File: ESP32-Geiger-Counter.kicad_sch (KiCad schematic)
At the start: 0 parts

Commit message: save
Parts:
- added J1: USB_C_Receptacle_PowerOnly_6P, symbol Connector:USB_C_Receptacle_PowerOnly_6P
- added U1: TP4056-42-ESOP8, Package_SO:SOIC-8-1EP_3.9x4.9mm_P1.27mm_EP2.41x3.3mm_ThermalVias, symbol Battery_Management:TP4056-42-ESOP8
- added U2: ESP32-WROOM-32, RF_Module:ESP32-WROOM-32, symbol RF_Module:ESP32-WROOM-32
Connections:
- new net: U2.1 (GND), U2.15 (GND), U2.38 (GND), U2.39 (GND)
- new net: J1.A12 (GND), J1.B12 (GND)
- new net: J1.A9 (VBUS), J1.B9 (VBUS)
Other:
- title: (none) -> ESP32-based Geiger Counter

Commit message: usb
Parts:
- removed J1: USB_C_Receptacle_PowerOnly_6P, symbol Connector:USB_C_Receptacle_PowerOnly_6P
- added BT1: Battery_Cell, Connector_JST:JST_PH_B2B-PH-K_1x02_P2.00mm_Vertical, symbol Device:Battery_Cell
- added J1: USB_C_Receptacle_USB2.0_16P, symbol Connector:USB_C_Receptacle_USB2.0_16P
- added R1, R2: 5.1K, symbol Device:R
- added U3: CP2102N-Axx-xQFN20, Package_DFN_QFN:SiliconLabs_QFN-20-1EP_3x3mm_P0.5mm, symbol Interface_USB:CP2102N-Axx-xQFN20
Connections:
- new net: J1.B5 (CC2), R2.1
- new net: J1.A5 (CC1), R1.1
- new net: U3.12 (GND), U3.21 (GND), U3.3 (GND)
- new net +3.3V: BT1.1 (+)
- new net +5V: J1.A4 (VBUS), J1.A9 (VBUS), J1.B4 (VBUS), J1.B9 (VBUS), U3.8 (VBUS)
- new net D+: J1.A6 (D+), J1.B6 (D+), U3.4 (D+)
- new net D-: J1.A7 (D-), J1.B7 (D-), U3.5 (D-)
- new net GND: BT1.2 (-), J1.A1 (GND), J1.A12 (GND), J1.B1 (GND), J1.B12 (GND), J1.SH (SHIELD), R1.2, R2.2
- no-connect marks 0 -> 2
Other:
- note added: "3.7V Lipo Cell"
- moved on the sheet: U1, U2

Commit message: saving
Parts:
- added C2: 10uF, symbol Device:C
- added C3: 100nF, symbol Device:C
- added F1: Polyfuse 500mA, Fuse:Fuse_1812_4532Metric, symbol Device:Polyfuse
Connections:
- net +5V: now also F1.1; no longer U3.8 (VBUS)
- net GND: now also U1.3 (GND), U1.9 (EPAD), C2.2, C3.2
- net VBUS_FUSED: now reaches U1.4 (V_{CC})
- net VBUS_FUSED: now also C2.1, C3.1, F1.2
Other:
- note added: "USB Input"
- moved on the sheet: BT1, U1, U2, U3

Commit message: working on TP4056
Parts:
- added D1: Red LED, symbol Device:LED
- added D2: Green LED, symbol Device:LED
- added R4: 2K, symbol Device:R
- added R5: 10K, symbol Device:R
- added R6, R7: 1K, symbol Device:R
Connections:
- net +3.3V is gone; now on net VBAT: BT1.1 (+)
- net VBUS_FUSED is gone; now on net +5V: C2.1, C3.1, F1.2, U1.4 (V_{CC})
- net +5V: now also U1.8 (CE), D1.2 (A), D2.2 (A), R5.2; no longer F1.1, J1.A4 (VBUS), J1.A9 (VBUS), J1.B4 (VBUS), J1.B9 (VBUS)
- net GND: now also R4.2
- net at U1.1 (TEMP): now also R5.1
- net at U1.2 (PROG): now also R4.1
- net VBAT: now reaches U1.5 (BAT)
- net at U1.6 (~{STDBY}): now also R7.2
- net at U1.7 (~{CHRG}): now also R6.2
- new net: D2.1 (K), R7.1
- new net: F1.1, J1.A4 (VBUS), J1.A9 (VBUS), J1.B4 (VBUS), J1.B9 (VBUS)
- new net: D1.1 (K), R6.1
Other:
- moved on the sheet: C2, C3, F1, U1, U2, U3

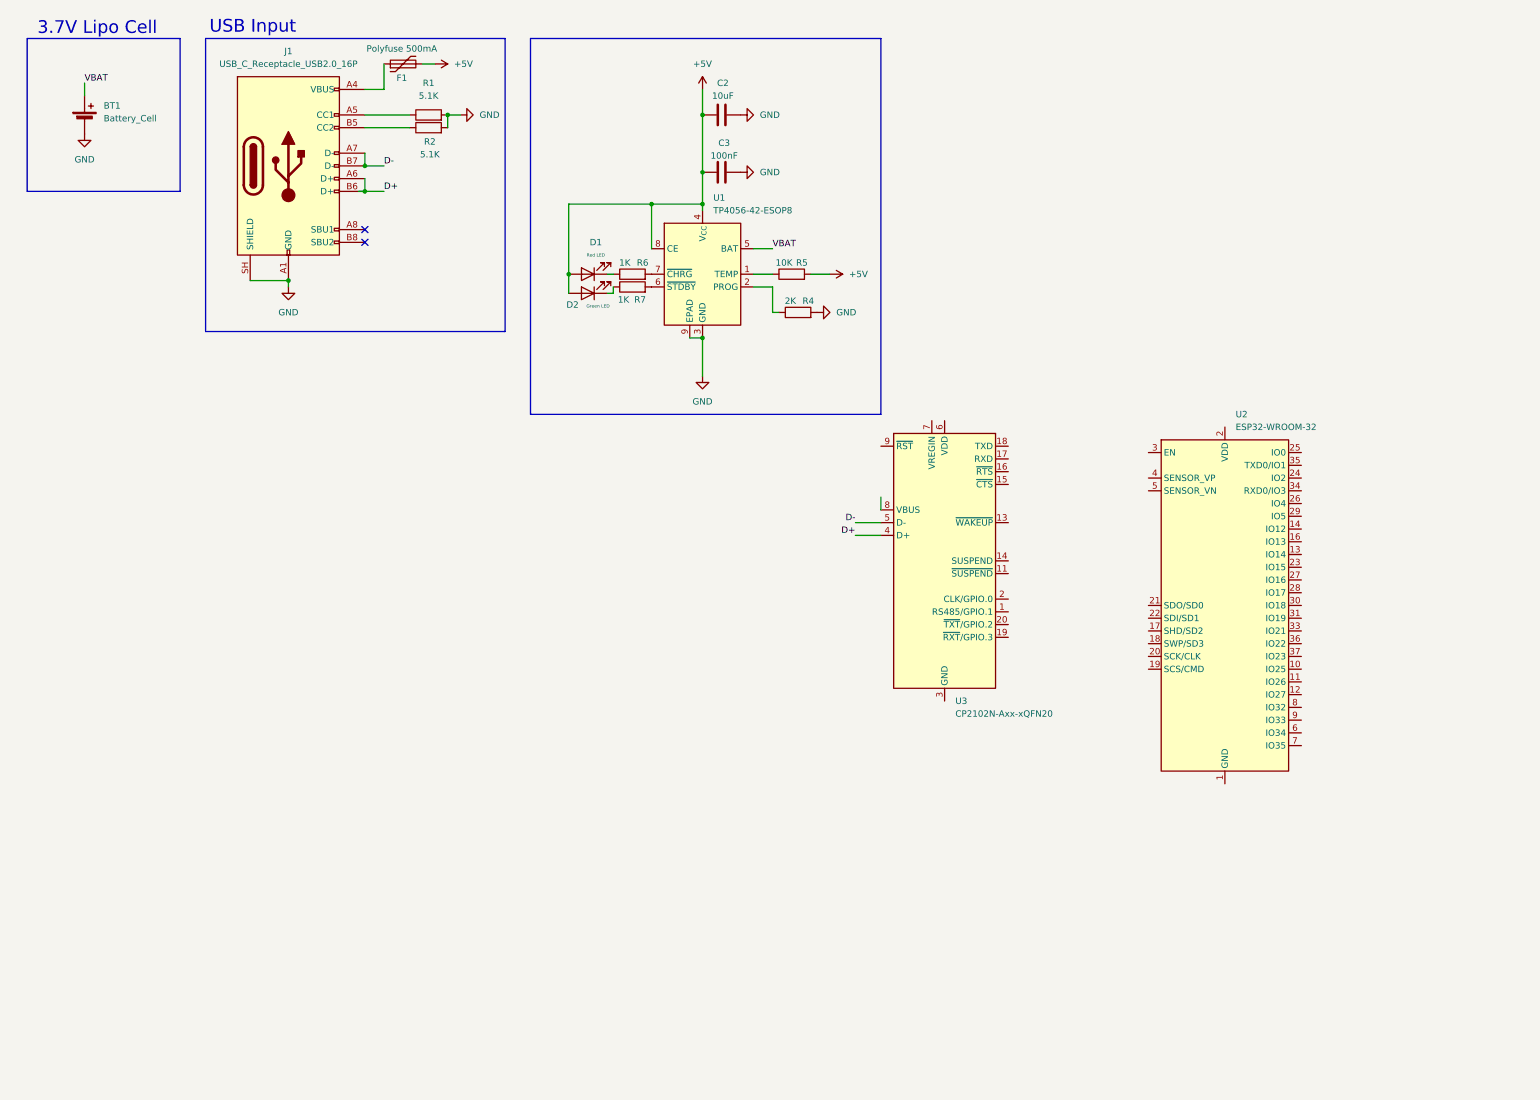
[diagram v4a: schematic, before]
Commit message: Lipo charging + usb input + lipo cell
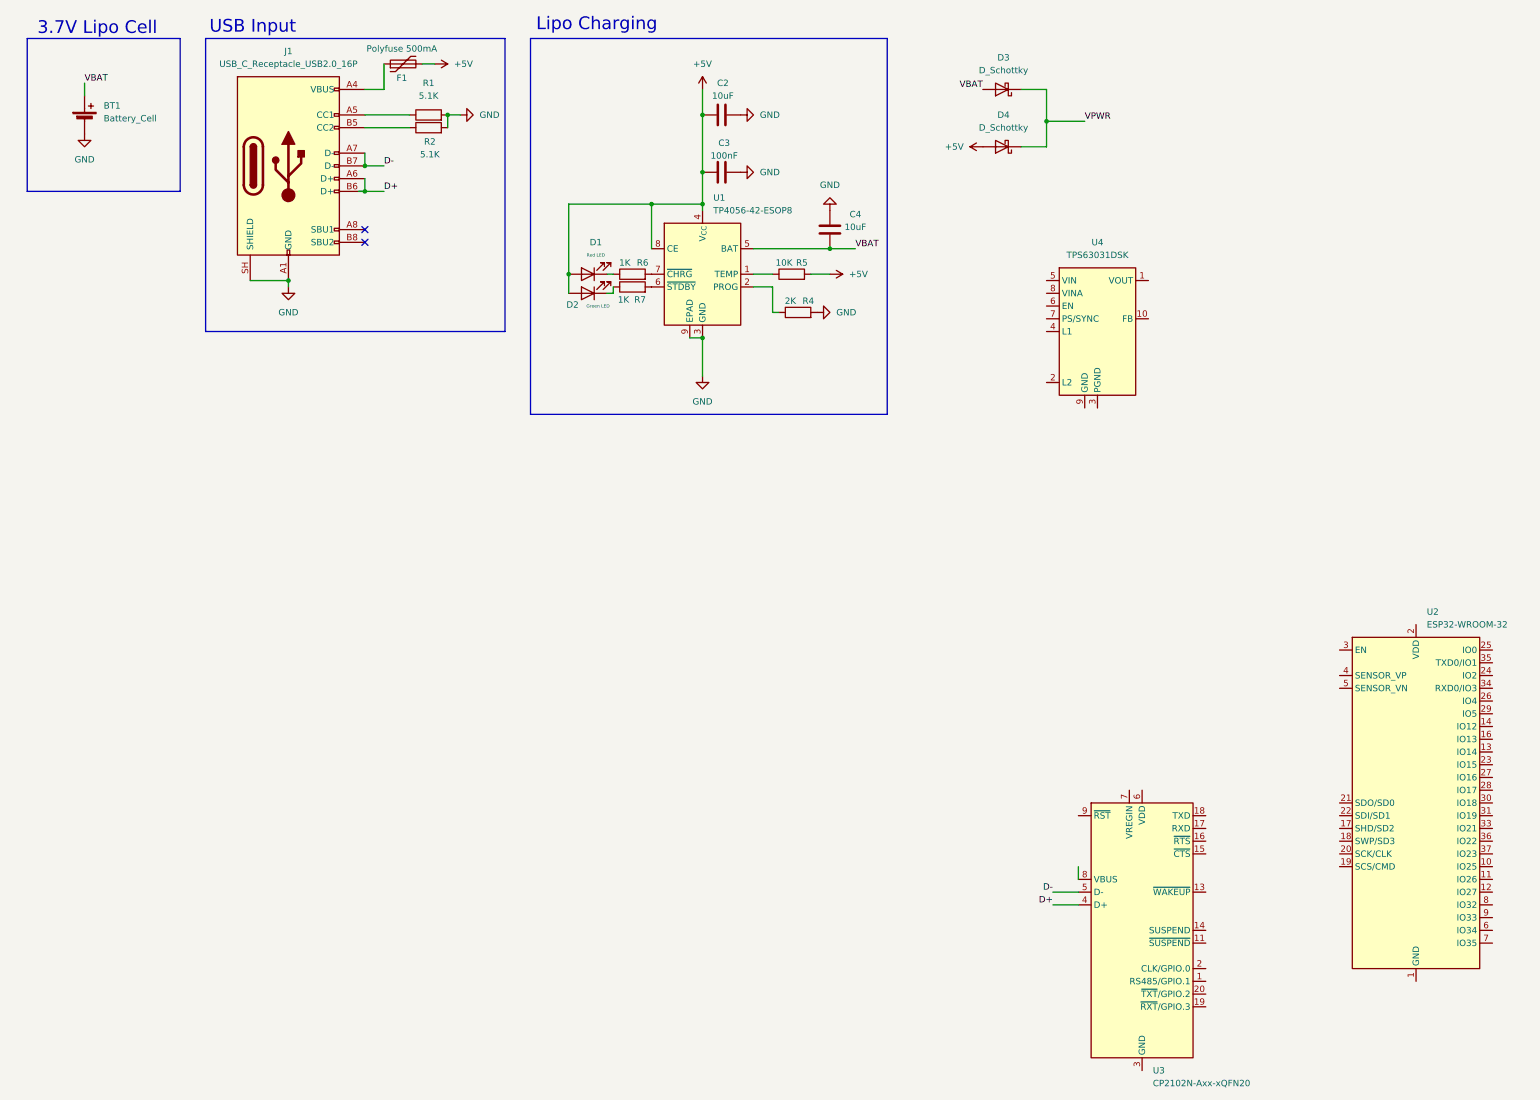
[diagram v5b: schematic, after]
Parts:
- added C4: 10uF, symbol Device:C
- added D3, D4: D_Schottky, symbol Device:D_Schottky
- added U4: TPS63031DSK, Package_SON:WSON-10-1EP_2.5x2.5mm_P0.5mm_EP1.2x2mm, symbol Regulator_Switching:TPS63031DSK
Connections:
- net +5V: now also D4.2 (A)
- net GND: now also C4.1
- net VBAT: now also C4.2, D3.2 (A)
- new net: U4.11 (PGND), U4.3 (PGND)
- new net VPWR: D3.1 (K), D4.1 (K)
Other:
- note added: "Lipo Charging"
- moved on the sheet: U2, U3

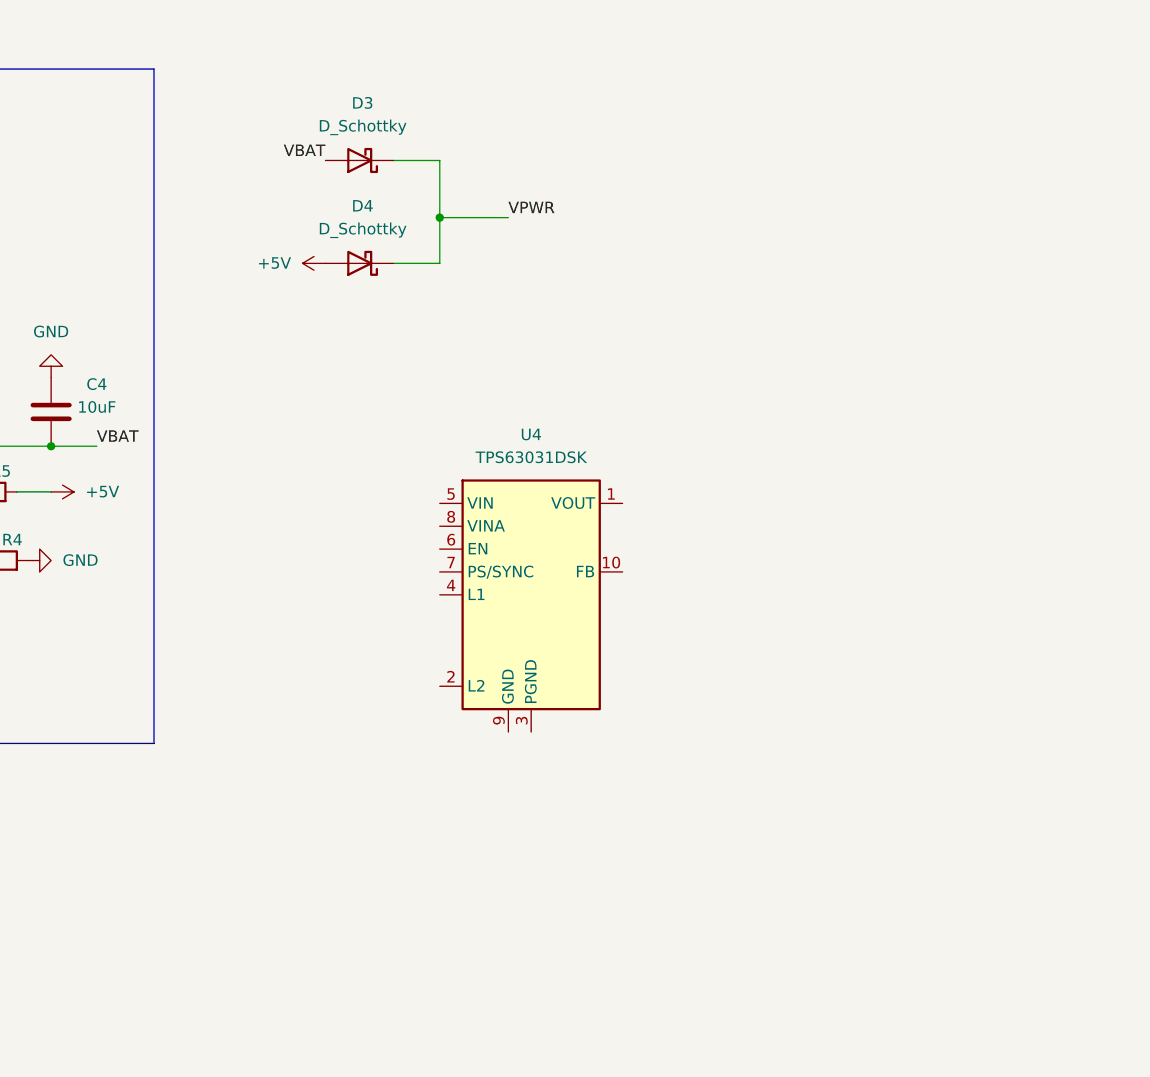
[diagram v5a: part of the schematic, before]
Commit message: buck boost added
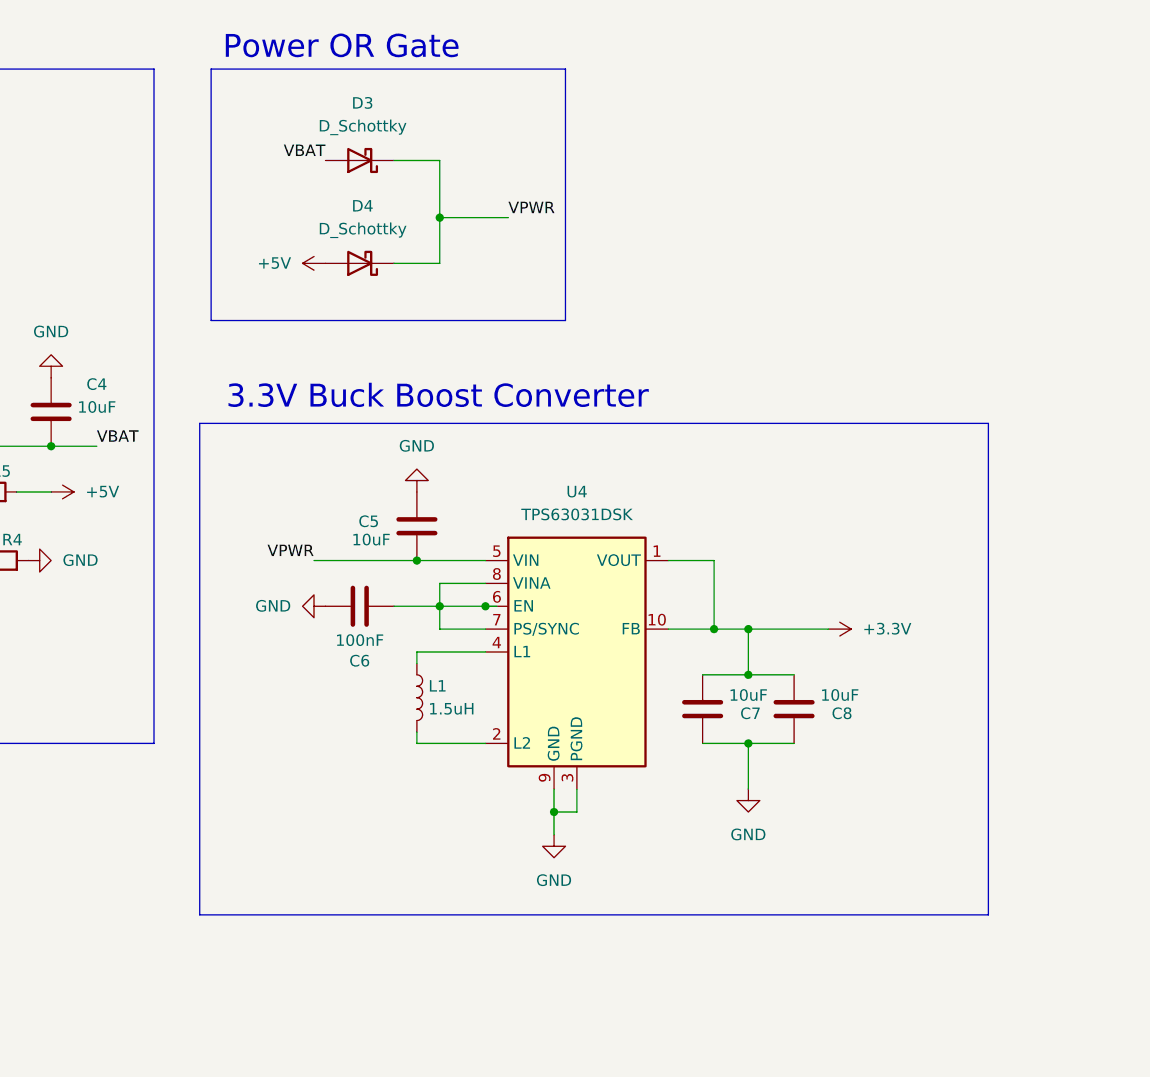
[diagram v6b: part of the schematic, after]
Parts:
- added C5, C7, C8: 10uF, symbol Device:C
- added C6: 100nF, symbol Device:C
- added L1: 1.5uH, symbol Device:L
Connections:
- net GND: now also U4.11 (PGND), U4.3 (PGND), U4.9 (GND), C5.2, C6.1, C7.2, C8.2
- net VPWR: now also U4.5 (VIN), C5.1
- net +3.3V: now reaches U4.1 (VOUT)
- net +3.3V: now also U4.10 (FB), C7.1, C8.1
- net at U4.2 (L2): now also L1.2
- net at U4.4 (L1): now also L1.1
- net at U4.6 (EN): now also U4.7 (PS/SYNC), U4.8 (VINA), C6.2
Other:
- note added: "3.3V Buck Boost Converter"
- note added: "Power OR Gate"
- moved on the sheet: U4
